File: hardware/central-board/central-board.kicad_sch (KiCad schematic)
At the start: 24 parts, among them J1 MTJ-88ARX1-FSM-LG, U1 MAX3485, U5 XC6220B331MR, U6 TPS5430DDAR

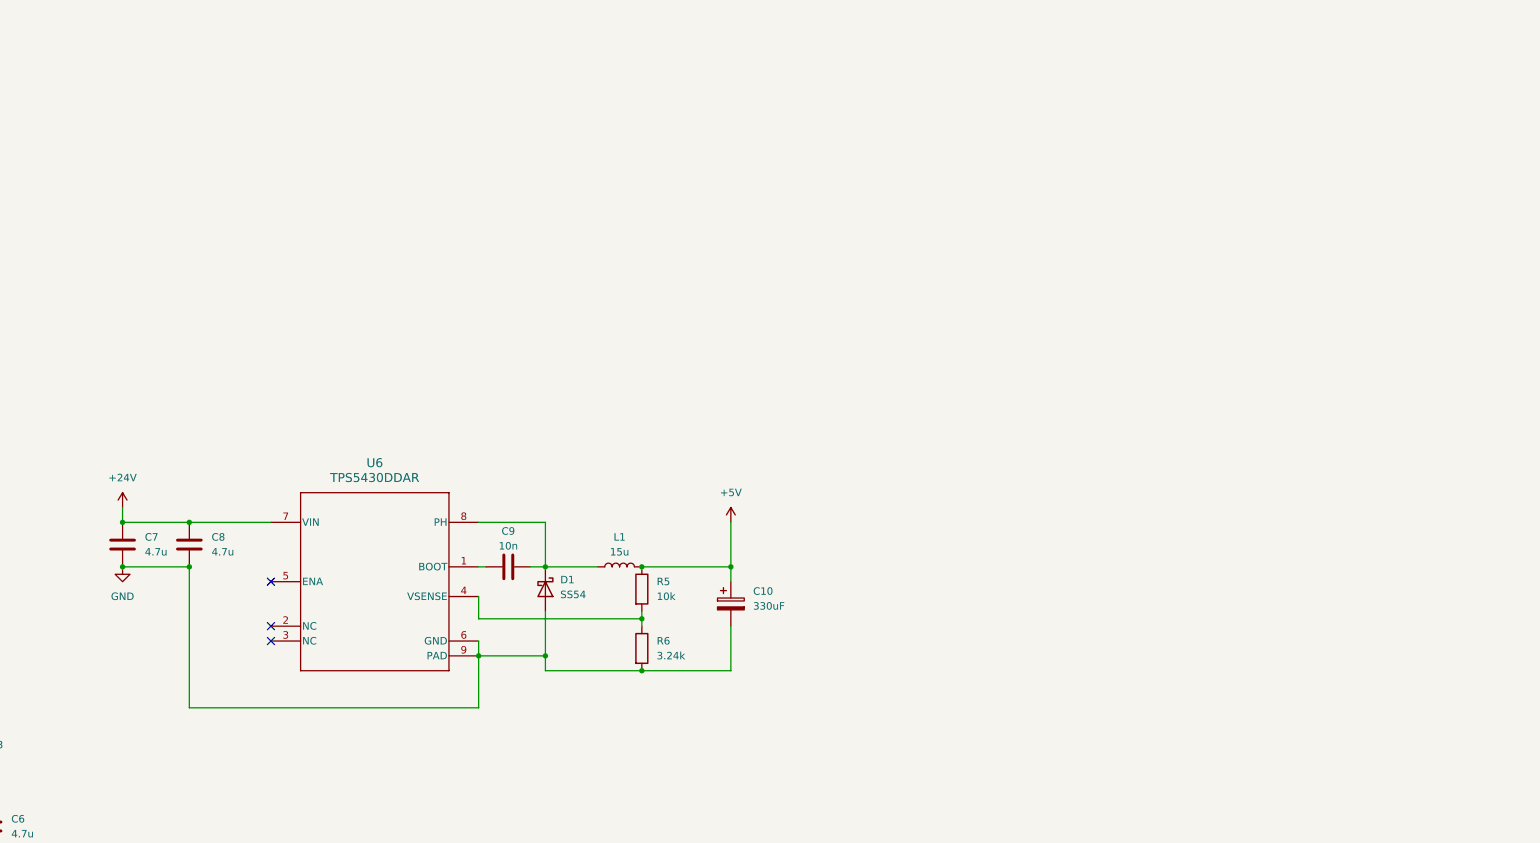
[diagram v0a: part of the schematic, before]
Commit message: Updates to buck, review TI
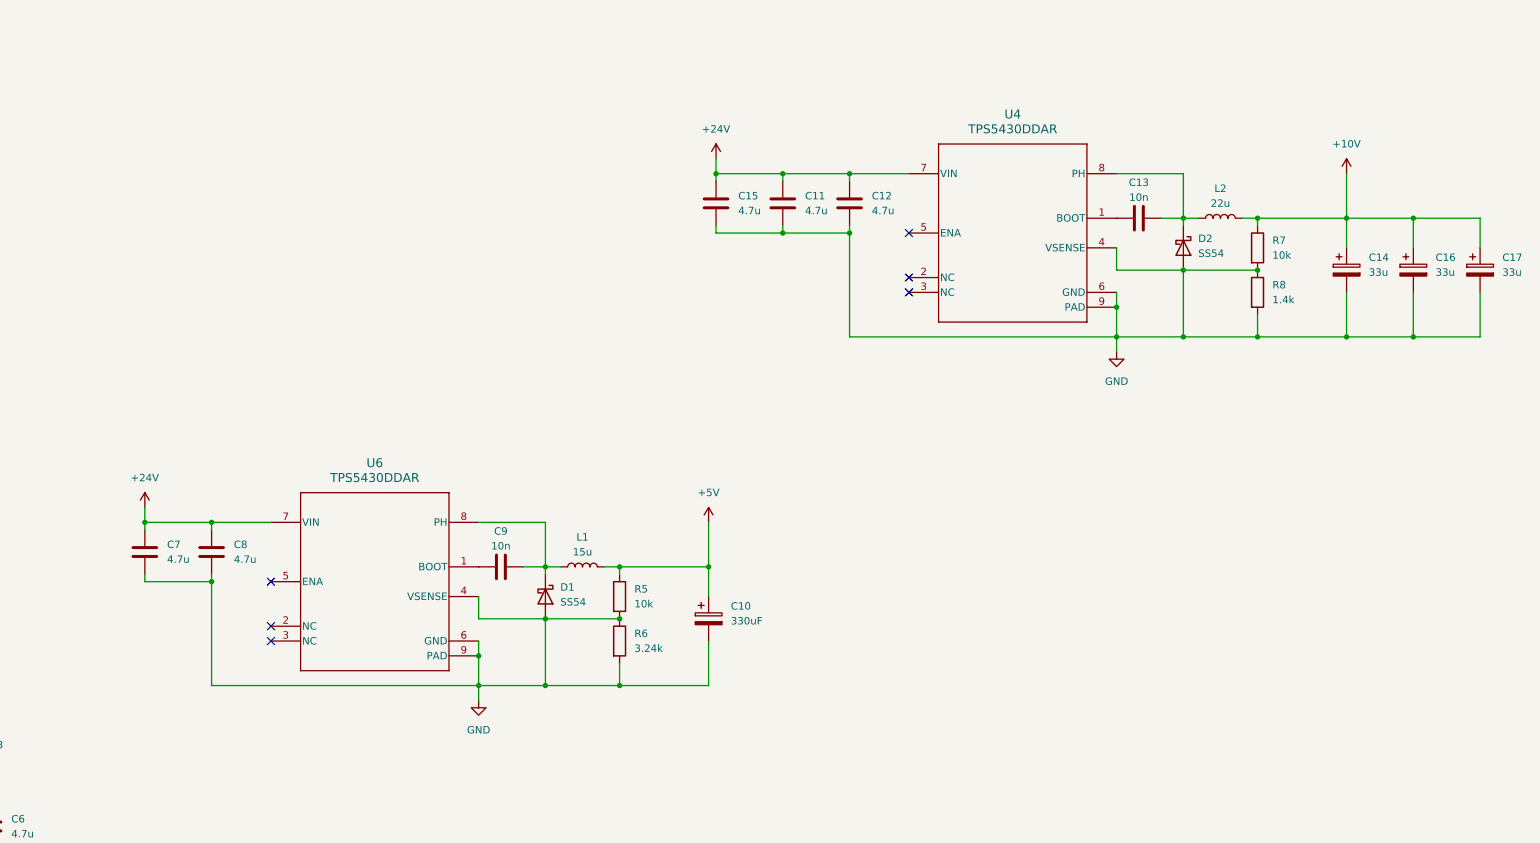
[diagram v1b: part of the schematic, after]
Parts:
- added C11, C12, C15: 4.7u, symbol Device:C
- added C13: 10n, symbol Device:C
- added C14, C16, C17: 33u, Capacitor_Tantalum_SMD:CP_EIA-7343-15_Kemet-W, symbol Device:C_Polarized
- added D2: SS54, Diode_SMD:D_SMA, symbol Device:D_Schottky
- added L2: 22u, symbol Device:L
- added R7: 10k, symbol Device:R
- added R8: 1.4k, symbol Device:R
- added U4: TPS5430DDAR, footprints:DDA0008J, symbol 2026-02-04_00-56-26:TPS5430DDAR
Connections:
- net +24V: now also C11.1, C12.1, C15.1, U4.7 (VIN)
- net GND: now also R5.2, R6.1, U6.4 (VSENSE), C11.2, C12.2, C14.2, C15.2, C16.2, C17.2, D2.2 (A), R7.2, R8.1, R8.2, U4.4 (VSENSE), U4.6 (GND), U4.9 (PAD)
- new net: C13.1, U4.1 (BOOT)
- new net: C13.2, D2.1 (K), L2.1, U4.8 (PH)
- new net +10V: C14.1, C16.1, C17.1, L2.2, R7.1
- no-connect marks 8 -> 11
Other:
- moved on the sheet: C10, C7, C8, C9, D1, L1, R5, R6

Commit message: updates to central
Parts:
- added J2, J3: 1729128, footprints:CONN_1729128_PXC, symbol 2026-02-04_18-40-10:1729128
- added J4: RPi_GPIO, footprints:RPI_Hat_B+, symbol RPi_Hat:RPi_GPIO
- added Q1, Q2, Q3: AO3400A, Package_TO_SOT_SMD:SOT-23, symbol Transistor_FET:AO3400A
- added R10, R11, R9: 100, symbol Device:R
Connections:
- net +10V is gone; now on net VBUS: C14.1, C16.1, C17.1, L2.2, R7.1
- net +24V: now also J2.1, J3.1
- net +5V: now also J4.2 (5V), J4.4 (5V)
- net BUSY: now also J4.18 (BCM24)
- net CS_1: now also J4.24 (BCM8_CE0)
- net DIO1: now also J4.16 (BCM23)
- net GND: now also J2.2, J4.14 (GND), J4.20 (GND), J4.25 (GND), J4.30 (GND), J4.34 (GND), J4.39 (GND), J4.6 (GND), J4.9 (GND), Q1.2 (S), Q2.2 (S), Q3.2 (S)
- net LED_GRN: now also J4.29 (BCM5)
- net LED_YLW: now also J4.31 (BCM6)
- net MISO: now also J4.21 (BCM9_MISO)
- net MOSI: now also J4.19 (BCM10_MOSI)
- net NRESET: now also J4.26 (BCM7_CE1)
- net RJ45_SNS: now also J4.33 (BCM13_PWM1)
- net RS_RX: now also J4.10 (BCM15_RXD)
- net SCK: now also J4.23 (BCM11_SCLK)
- net VBUS_EN: now reaches U4.5 (ENA)
- net VBUS_EN: now also J4.36 (BCM16)
- new net: Q1.1 (G), R9.2
- new net: Q2.1 (G), R10.2
- new net: Q3.1 (G), R11.2
- new net -LED: J3.2, Q1.3 (D), Q2.3 (D), Q3.3 (D)
- new net PWM: J4.32 (BCM12_PWM0), R10.1, R11.1, R9.1
- new net SCL: J4.5 (BCM3_SCL)
- new net SDA: J4.3 (BCM2_SDA)
- no-connect marks 11 -> 15
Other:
- note added: "+3V3 LDO"
- note added: "+5V Buck"
- note added: "I/O COMPONENTS"
- note added: "LED DRIVER"
- note added: "POWER SYSTEMS"
- note added: "VBUS (+10V) BUCK"
- moved on the sheet: C1, C10, C11, C12, C13, C14, C15, C16, C17, C2, C3, C4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

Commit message: Satelite & Central Schematic Finished
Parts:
- added C18, C19: 10n, symbol Device:C
- added J10, J11, J8: Conn_01x02, symbol Connector_Generic:Conn_01x02
- added J5: PEC11R, symbol Connector_Generic:Conn_01x03
- added J6: IO Power Bus, symbol Connector_Generic:Conn_02x05_Counter_Clockwise
- added J7: IO I2C Bus, symbol Connector_Generic:Conn_02x03_Counter_Clockwise
- added J9: GPIO Bus, symbol Connector_Generic:Conn_02x03_Counter_Clockwise
- added Q4, Q5, Q6: AO3400A, Package_TO_SOT_SMD:SOT-23, symbol Transistor_FET:AO3400A
- added R12, R13, R14, R15: 10k, symbol Device:R
- added R16, R17, R18: 100, symbol Device:R
- C14, C16, C17: value 33u -> 22u
- J1: footprint MTJ-88ARX1-FSM-LG:ADAMTECH_MTJ-88ARX1-FSM-LG -> footprints:ADAMTECH_MTJ-88ARX1-FSM-LG
- R8: value 1.4k -> 1.13k
- U2: footprint ProLib_pcs_2026-01-30:WIRELM-SMD_16P-L16.0-W16.0-P2.00_LORA-CC68-915MHZ-TCXO -> footprints:WIRELM-SMD_16P-L16.0-W16.0-P2.00_LORA-CC68-915MHZ-TCXO
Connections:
- net +3.3V is gone; now on net +3V3: C3.1, C4.1, U1.8 (VCC)
- net +3V3: now also J6.10 (Pin_10), J6.6 (Pin_6), J6.7 (Pin_7), J6.8 (Pin_8), J6.9 (Pin_9), R12.1, R13.1
- net GND: now also C18.2, C19.2, J5.3 (Pin_3), J6.1 (Pin_1), J6.2 (Pin_2), J6.3 (Pin_3), J6.4 (Pin_4), J6.5 (Pin_5), Q4.2 (S), Q5.2 (S), Q6.2 (S)
- net SCL: now also J7.1 (Pin_1), J7.2 (Pin_2), J7.3 (Pin_3)
- net SDA: now also J7.4 (Pin_4), J7.5 (Pin_5), J7.6 (Pin_6)
- net GPIO17: now reaches J4.11 (BCM17)
- net GPIO17: now also J9.6 (Pin_6)
- net GPIO18: now reaches J4.12 (BCM18_PCM_C)
- net GPIO18: now also J9.2 (Pin_2)
- net EN_S2: now reaches J4.13 (BCM27)
- net EN_S2: now also R16.1
- net EN_S3: now reaches J4.15 (BCM22)
- net EN_S3: now also R17.1
- net EN_S1: now reaches J4.22 (BCM25)
- net EN_S1: now also R18.1
- net GPIO19: now reaches J4.35 (BCM19_MISO_PCM_FS)
- net GPIO19: now also J9.5 (Pin_5)
- net GPIO26: now reaches J4.37 (BCM26)
- net GPIO26: now also J9.1 (Pin_1)
- net GPIO20: now reaches J4.38 (BCM20_MOSI_PCM_DI)
- net GPIO20: now also J9.3 (Pin_3)
- net GPIO21: now reaches J4.40 (BCM21_SCLK_PCM_DO)
- net GPIO21: now also J9.4 (Pin_4)
- net VBUS renamed +12V
- net +12V: now also J10.1 (Pin_1), J11.1 (Pin_1), J8.1 (Pin_1)
- new net: J5.1 (Pin_1), R12.2, R14.2
- new net: Q6.1 (G), R18.2
- new net: J8.2 (Pin_2), Q6.3 (D)
- new net: Q5.1 (G), R17.2
- new net: J11.2 (Pin_2), Q5.3 (D)
- new net: Q4.1 (G), R16.2
- new net: J10.2 (Pin_2), Q4.3 (D)
- new net: J5.2 (Pin_2), R13.2, R15.2
- new net KNOB_A: C19.1, R14.1
- new net KNOB_B: C18.1, R15.1
- no-connect marks 15 -> 16
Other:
- note added: "+12V Buck"
- note added: "FRONT I/O HEADERS"
- note added: "PI HAT HEADER"
- note added: "RJ45 Connector"
- note added: "RS-485 UART Transciever"
- note added: "SOLENOID DRIVER"
- note removed: "VBUS (+10V) BUCK"
- moved on the sheet: C1, C10, C11, C12, C13, C14, C15, C16, C17, C2, C3, C4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

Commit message: LCSC Updates
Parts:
- removed J6: IO Power Bus, symbol Connector_Generic:Conn_02x05_Counter_Clockwise
- removed J7: IO I2C Bus, symbol Connector_Generic:Conn_02x03_Counter_Clockwise
- removed J9: GPIO Bus, symbol Connector_Generic:Conn_02x03_Counter_Clockwise
- added J12: IO I2C Bus, Connector_PinHeader_2.54mm:PinHeader_2x03_P2.54mm_Vertical, symbol Connector_Generic:Conn_02x03_Odd_Even
- added J7: GPIO Bus, Connector_PinHeader_2.54mm:PinHeader_2x03_P2.54mm_Vertical, symbol Connector_Generic:Conn_02x03_Odd_Even
- added J9: IO Power Bus, Connector_PinHeader_2.54mm:PinHeader_2x05_P2.54mm_Vertical, symbol Connector_Generic:Conn_02x05_Odd_Even
- C1, C3: footprint (none) -> Capacitor_SMD:C_0402_1005Metric; LCSC (none) -> C1525
- C10: value 330uF -> 330u; LCSC (none) -> C2158135
- C11, C12, C15, C4, C6, C7, C8: footprint (none) -> Capacitor_SMD:C_0805_2012Metric; LCSC (none) -> C1779
- C13, C18, C19, C9: footprint (none) -> Capacitor_SMD:C_0402_1005Metric; LCSC (none) -> C15195
- C14, C16, C17: LCSC (none) -> C308917
- C2, C5: footprint (none) -> Capacitor_SMD:C_0603_1608Metric; LCSC (none) -> C19702
- D1, D2: LCSC (none) -> C22452
- J10, J11, J8: footprint (none) -> Connector_PinHeader_2.54mm:PinHeader_1x02_P2.54mm_Vertical
- J2, J3: LCSC (none) -> C7509570
- J5: footprint (none) -> Connector_PinHeader_2.54mm:PinHeader_1x03_P2.54mm_Vertical
- Q1, Q2, Q3, Q4, Q5, Q6: LCSC (none) -> C20917
- R1: footprint (none) -> Resistor_SMD:R_0805_2012Metric; LCSC (none) -> C17437
- R10, R11, R16, R17, R18, R9: footprint (none) -> Resistor_SMD:R_0603_1608Metric; LCSC (none) -> C22775
- R12, R13, R14, R15, R5, R7: footprint (none) -> Resistor_SMD:R_0603_1608Metric; LCSC (none) -> C25804
- R2, R3: footprint (none) -> Resistor_SMD:R_0603_1608Metric; LCSC (none) -> C22808
- R4: footprint (none) -> Resistor_SMD:R_0402_1005Metric; LCSC (none) -> C11702
- R6: value 3.24k -> 3.3k; footprint (none) -> Resistor_SMD:R_0603_1608Metric; LCSC (none) -> C22978
- R8: value 1.13k -> 1.2k; footprint (none) -> Resistor_SMD:R_0805_2012Metric; LCSC (none) -> C17379
- U1: LCSC (none) -> C668204
- U2: LCSC (none) -> C5356643
- U3: LCSC (none) -> C7498154
- U4, U6: LCSC (none) -> C9864
- U5: LCSC (none) -> C86534
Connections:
- net +3V3: now also J9.10 (Pin_10), J9.2 (Pin_2), J9.4 (Pin_4), J9.6 (Pin_6), J9.8 (Pin_8)
- net GND: now also J9.1 (Pin_1), J9.3 (Pin_3), J9.5 (Pin_5), J9.7 (Pin_7), J9.9 (Pin_9)
- net GPIO17: now also J7.2 (Pin_2)
- net GPIO18: now also J7.3 (Pin_3)
- net GPIO19: now also J7.4 (Pin_4)
- net GPIO20: now also J7.5 (Pin_5)
- net GPIO21: now also J7.6 (Pin_6)
- net GPIO26: now also J7.1 (Pin_1)
- net SCL: now also J12.1 (Pin_1), J12.3 (Pin_3), J12.5 (Pin_5)
- net SDA: now also J12.2 (Pin_2), J12.4 (Pin_4), J12.6 (Pin_6)

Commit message: Primary Board PCB Updates
2 bucks finished
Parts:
- C11, C12, C15, C7, C8: footprint Capacitor_SMD:C_0805_2012Metric -> Capacitor_SMD:C_1206_3216Metric; LCSC C1779 -> C29823
- C2: footprint Capacitor_SMD:C_0603_1608Metric -> Capacitor_SMD:C_0402_1005Metric; LCSC C19702 -> C15525
- C4, C6: footprint Capacitor_SMD:C_0805_2012Metric -> Capacitor_SMD:C_0402_1005Metric; LCSC C1779 -> C23733
- D1, D2: value SS54 -> ~; footprint Diode_SMD:D_SMA -> Diode_SMD:SOD-123_L2.6-W1.6-LS3.5-RD; LCSC C22452 -> C489144
- L1: value 15u -> 22u; footprint (none) -> Library:IND-SMD_L11.5-W10.0; LCSC (none) -> C842886
- L2: footprint (none) -> Library:IND-SMD_L11.5-W10.0; LCSC (none) -> C842886
- R1: footprint Resistor_SMD:R_0805_2012Metric -> Resistor_SMD:R_0402_1005Metric; LCSC C17437 -> C25079
- R12, R13, R14, R15, R5, R7: footprint Resistor_SMD:R_0603_1608Metric -> Resistor_SMD:R_0402_1005Metric; LCSC C25804 -> C25744
- R6: footprint Resistor_SMD:R_0603_1608Metric -> Resistor_SMD:R_0402_1005Metric; LCSC C22978 -> C25890
- R8: footprint Resistor_SMD:R_0805_2012Metric -> Resistor_SMD:R_0603_1608Metric; LCSC C17379 -> C22765
- U3: footprint 123-02-01:SMA-TH_SMA-KWE_C7498154 -> footprints:SMA-TH_SMA-KWE_C7498154
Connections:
- net GND: no longer R5.2, R6.1, R7.2, R8.1, U4.4 (VSENSE), U6.4 (VSENSE)
- new net: R5.2, R6.1, U6.4 (VSENSE)
- new net: R7.2, R8.1, U4.4 (VSENSE)
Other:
- moved on the sheet: D1, D2

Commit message: more updates
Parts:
- removed J9: IO Power Bus, Connector_PinHeader_2.54mm:PinHeader_2x05_P2.54mm_Vertical, symbol Connector_Generic:Conn_02x05_Odd_Even
- added J6: IO Power Bus, Connector_PinHeader_2.54mm:PinHeader_2x03_P2.54mm_Vertical, symbol Connector_Generic:Conn_02x03_Odd_Even
- J7: footprint Connector_PinHeader_2.54mm:PinHeader_2x03_P2.54mm_Vertical -> Connector_PinHeader_2.54mm:PinHeader_1x06_P2.54mm_Vertical
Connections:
- net +3V3: now also J6.2 (Pin_2), J6.4 (Pin_4), J6.6 (Pin_6)
- net BUSY: now also J4.38 (BCM20_MOSI_PCM_DI); no longer J4.18 (BCM24)
- net DIO1: now also J4.40 (BCM21_SCLK_PCM_DO); no longer J4.16 (BCM23)
- net EN_S1: now also J4.8 (BCM14_TXD); no longer J4.22 (BCM25)
- net EN_S2: now also J4.7 (BCM4_GPCLK0); no longer J4.13 (BCM27)
- net EN_S3: now also J4.11 (BCM17); no longer J4.15 (BCM22)
- net GND: now also J6.1 (Pin_1), J6.3 (Pin_3), J6.5 (Pin_5)
- net GPIO17: now also J4.36 (BCM16), J7.5 (Pin_5); no longer J4.11 (BCM17), J7.2 (Pin_2)
- net GPIO18: now also J4.33 (BCM13_PWM1); no longer J4.12 (BCM18_PCM_C)
- net GPIO20: now also J4.31 (BCM6), J7.2 (Pin_2); no longer J4.38 (BCM20_MOSI_PCM_DI), J7.5 (Pin_5)
- net GPIO21: now also J4.29 (BCM5), J7.1 (Pin_1); no longer J4.40 (BCM21_SCLK_PCM_DO), J7.6 (Pin_6)
- net GPIO26: now also J7.6 (Pin_6); no longer J7.1 (Pin_1)
- net LED_GRN: no longer J4.29 (BCM5)
- net LED_YLW: no longer J4.31 (BCM6)
- net RJ45_SNS: now also J4.12 (BCM18_PCM_C); no longer J4.33 (BCM13_PWM1)
- net VBUS_EN: no longer names the net of U4.5 (ENA)
- net VBUS_EN: no longer J4.36 (BCM16)
- no-connect marks 16 -> 15
